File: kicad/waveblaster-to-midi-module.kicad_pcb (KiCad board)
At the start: 2 copper layers, 33 x 95 mm, 14 parts, among them J1 Midi Out, J2 Midi In, J3 Right In, J4 Left In, J5 Right Out, J6 Left Out, J7 Wavetable Input, U1 H11L1

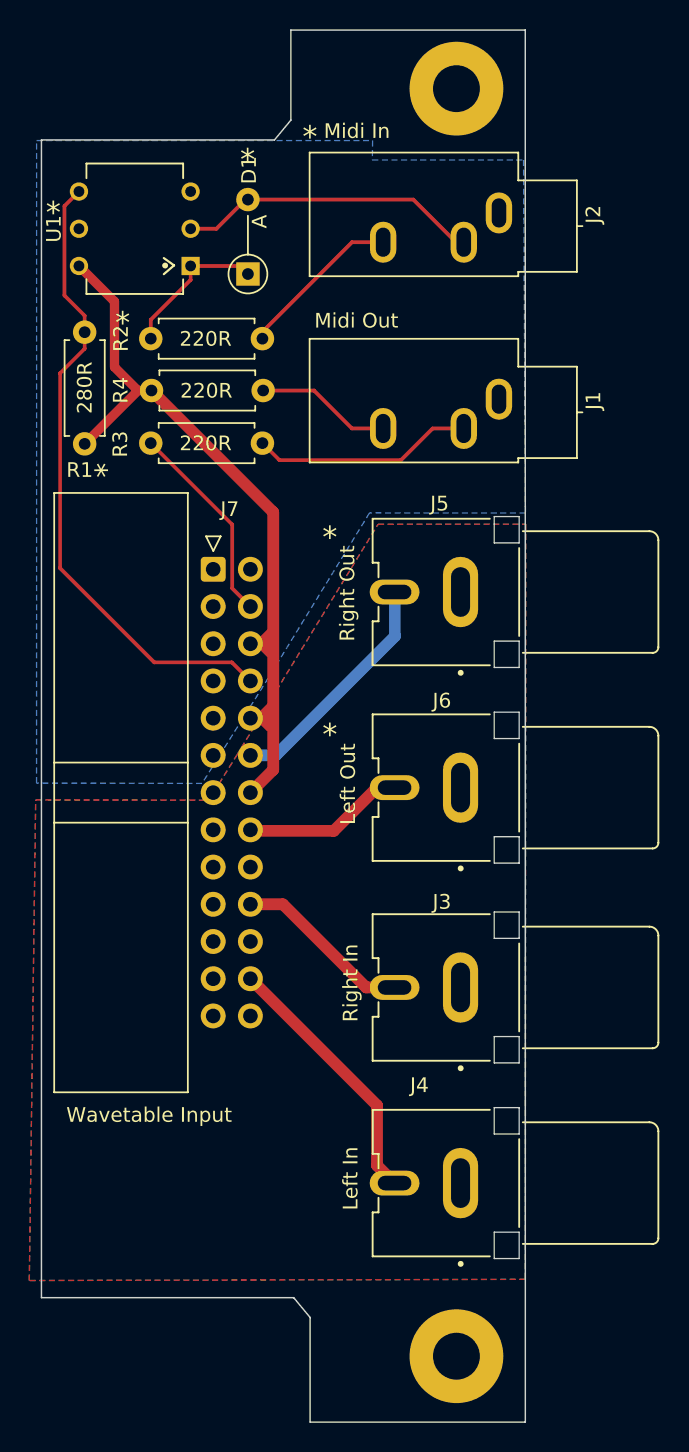
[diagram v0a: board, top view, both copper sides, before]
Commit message: fix clearance issues, fix bracket
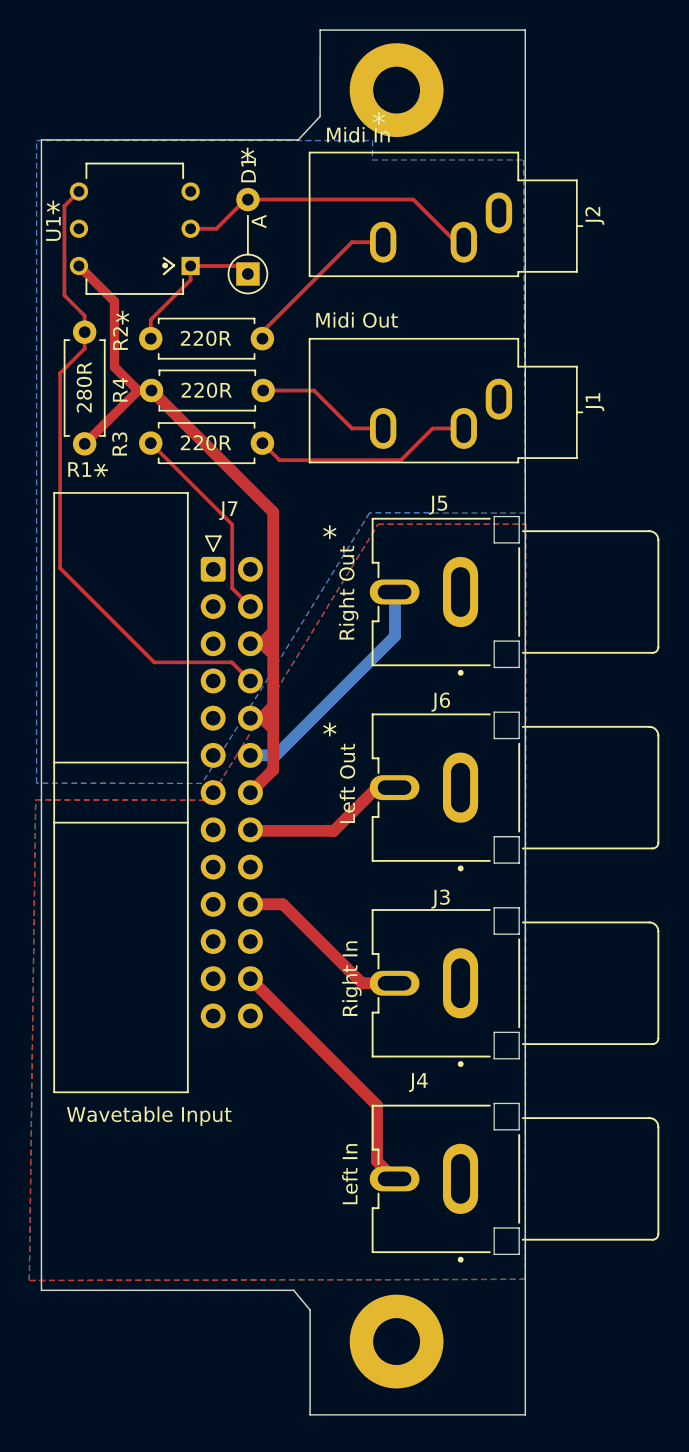
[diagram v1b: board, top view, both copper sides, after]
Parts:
- moved H1 4.09 mm to (181.2, 57.1)
- moved J3 0.29 mm to (189.6, 118.0)
- moved J4 0.29 mm to (189.6, 131.4)
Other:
- board size 33 x 95 mm -> 33 x 94.5 mm
- board text added: "Waveblaster Breakout Card v1.1 by Nikitalita"
- board text removed: "Waveblaster Breakout Card v1.0 by Nikitalita"
